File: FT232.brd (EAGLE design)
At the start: 100 x 80 mm, 17 parts, among them J1 USB, J2 CON, U1 FT232, Y1 CRYSTAL

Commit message: 第二次布线尝试
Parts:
- J1: value USB -> USBA; device FT232:USB_SMD -> FT232:USB_A
- moved Z1 5.08 mm to (17.8, 5.08)
- moved R3 2.54 mm to (14.0, 7.62)
- moved Z2 2.54 mm to (17.8, 7.62)
- moved Z3 2.54 mm to (17.8, 10.2)
- moved C4 2.54 mm to (14.0, 6.35)
- moved R4 1.27 mm to (14.0, 8.89)
- moved R1 1.27 mm to (14.0, 3.81)
- moved R2 1.27 mm to (14.0, 5.08)
- moved R5 1.27 mm to (14.0, 10.2)
- turned J1 to 270 degrees
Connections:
- net N$1 renamed D_N
- net N$2 renamed D_P
- net +5V: now also J1.VBUS; no longer J1.VCC
- net GND: now also J1.GND1, J1.GND2
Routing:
- net +5V: track 0.00 -> 59.6 mm, vias 0 -> 4
- net RXD: track 0.00 -> 14.0 mm, vias 0 -> 1
- net N$8: track 0.00 -> 12.0 mm, vias 0 -> 2
- net TXD: track 0.00 -> 10.2 mm, vias 0 -> 1
- net D_N: track 0.00 -> 9.85 mm
- net N$9: track 0.00 -> 9.81 mm, vias 0 -> 2
- net N$7: track 0.00 -> 9.67 mm
- net D_P: track 0.00 -> 9.28 mm
- net N$6: track 0.00 -> 9.15 mm
- net N$5: track 0.00 -> 8.30 mm
- net N$4: track 0.00 -> 7.19 mm
- net N$3: track 0.00 -> 7.19 mm
- net N$12: track 0.00 -> 4.53 mm, vias 0 -> 2
- net N$11: track 0.00 -> 2.74 mm
- net GND: track 0.00 -> 2.45 mm, vias 0 -> 3
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- added copper zone on layer 1, net GND
- added copper zone on layer 16, net GND
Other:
- board size 100 x 80 mm -> 29.2 x 12 mm

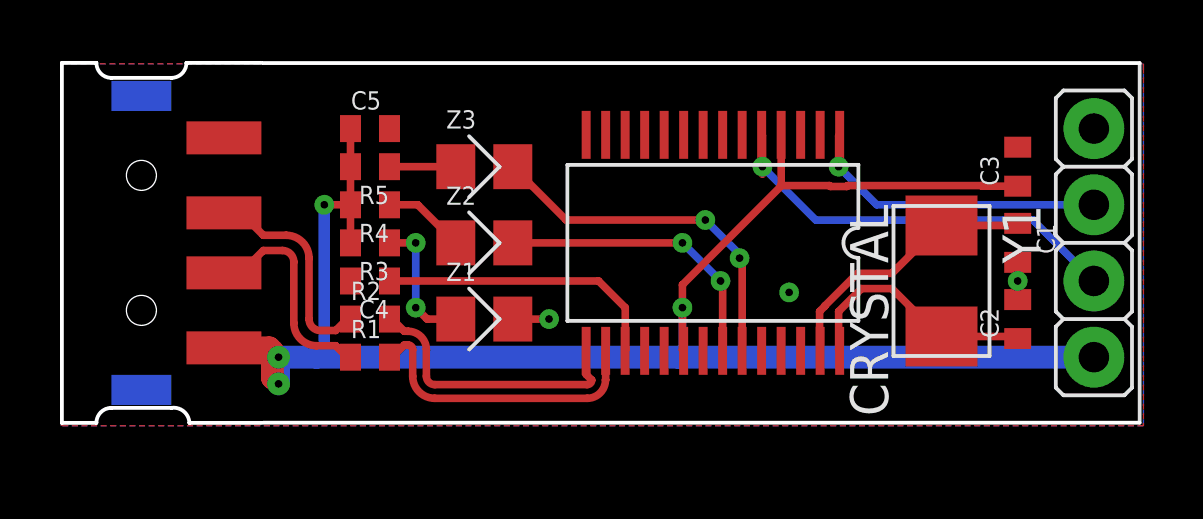
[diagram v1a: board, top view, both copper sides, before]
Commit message: 增加一个过孔
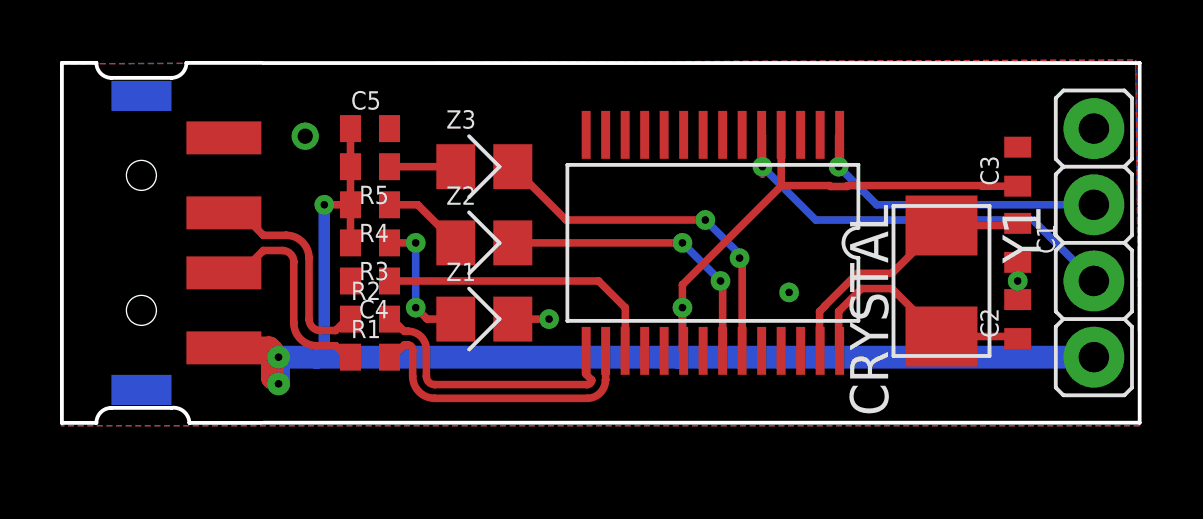
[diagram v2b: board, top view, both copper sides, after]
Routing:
- net GND: vias 3 -> 4
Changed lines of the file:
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@@
 <?xml version="1.0" encoding="utf-8"?>
 <!DOCTYPE eagle SYSTEM "eagle.dtd">
-<eagle version="8.1.0">
+<eagle version="7.7.0">
 <drawing>
 <settings>
@@
 <plain>
 <wire x1="10.414" y1="13.6144" x2="39.624" y2="13.6144" width="0.127" layer="20"/>
-<wire x1="39.624" y1="13.6144" x2="39.624" y2="1.6256" width="0.127" layer="21"/>
+<wire x1="39.624" y1="13.6144" x2="39.624" y2="1.6256" width="0.127" layer="20"/>
 <wire x1="39.624" y1="1.6256" x2="10.414" y2="1.6256" width="0.127" layer="20"/>
 </plain>
@@
 <polygon width="0.254" layer="16">
 <vertex x="3.683" y="13.589"/>
-<vertex x="39.751" y="13.589"/>
-<vertex x="39.751" y="1.524"/>
+<vertex x="39.497" y="13.716"/>
+<vertex x="39.624" y="1.524"/>
 <vertex x="3.683" y="1.524"/>
 </polygon>
 <polygon width="0.254" layer="1">
 <vertex x="3.683" y="13.589"/>
-<vertex x="39.751" y="13.589"/>
-<vertex x="39.751" y="13.462"/>
-<vertex x="39.751" y="1.524"/>
+<vertex x="39.497" y="13.716"/>
+<vertex x="39.497" y="13.589"/>
+<vertex x="39.624" y="1.524"/>
 <vertex x="3.683" y="1.524"/>
 </polygon>
 <via x="27.94" y="5.969" extent="1-16" drill="0.254" diameter="0.254"/>
-<wire x1="27.675" y1="4.02" x2="27.94" y2="5.969" width="0" layer="19" extent="1-1"/>
+<via x="11.811" y="11.176" extent="1-16" drill="0.508" diameter="0.508"/>
+<wire x1="35.56" y1="10.81" x2="38.1" y2="11.43" width="0" layer="19" extent="1-1"/>
+<wire x1="35.56" y1="6.97" x2="35.56" y2="10.81" width="0" layer="19" extent="1-1"/>
+<wire x1="28.325" y1="4.02" x2="35.56" y2="5.73" width="0" layer="19" extent="1-1"/>
+<wire x1="27.675" y1="4.02" x2="28.325" y2="4.02" width="0" layer="19" extent="1-1"/>
+<wire x1="27.94" y1="5.969" x2="27.675" y2="4.02" width="0" layer="19" extent="1-1"/>
+<wire x1="25.075" y1="4.02" x2="27.675" y2="4.02" width="0" layer="19" extent="1-1"/>
+<wire x1="23.125" y1="4.02" x2="25.075" y2="4.02" width="0" layer="19" extent="1-1"/>
+<wire x1="19.939" y1="5.08" x2="23.125" y2="4.02" width="0" layer="19" extent="1-1"/>
+<wire x1="13.32" y1="6.35" x2="18.73" y2="5.08" width="0" layer="19" extent="1-1"/>
+<wire x1="11.811" y1="11.176" x2="13.32" y2="6.35" width="0" layer="19" extent="1-1"/>
+<wire x1="9.1" y1="11.12" x2="11.811" y2="11.176" width="0" layer="19" extent="1-1"/>
+<wire x1="14.62" y1="11.43" x2="11.811" y2="11.176" width="0" layer="19" extent="1-1"/>
+<wire x1="6.35" y1="12.52" x2="9.1" y2="11.12" width="0" layer="19" extent="1-16"/>
+<wire x1="25.725" y1="11.22" x2="27.94" y2="5.969" width="0" layer="19" extent="1-1"/>
+<wire x1="6.35" y1="2.72" x2="13.32" y2="6.35" width="0" layer="19" extent="1-16"/>
 </signal>
 <signal name="+5V">
